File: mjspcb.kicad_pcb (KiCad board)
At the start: 2 copper layers, 97.2 x 55.9 mm, 77 parts, among them P10 Lipo, P2 serial breakout, P3 I2C breakout, P4 GPS, P5 piezo, P6 BPW34, P7 electrodes, P8 perfboard breakout, P9 reset, Q1 STU60N3LH5, Q2 STU60N3LH5, U1 ATMEGA328P, U2 RFM95W, U3 MCP1700-3302

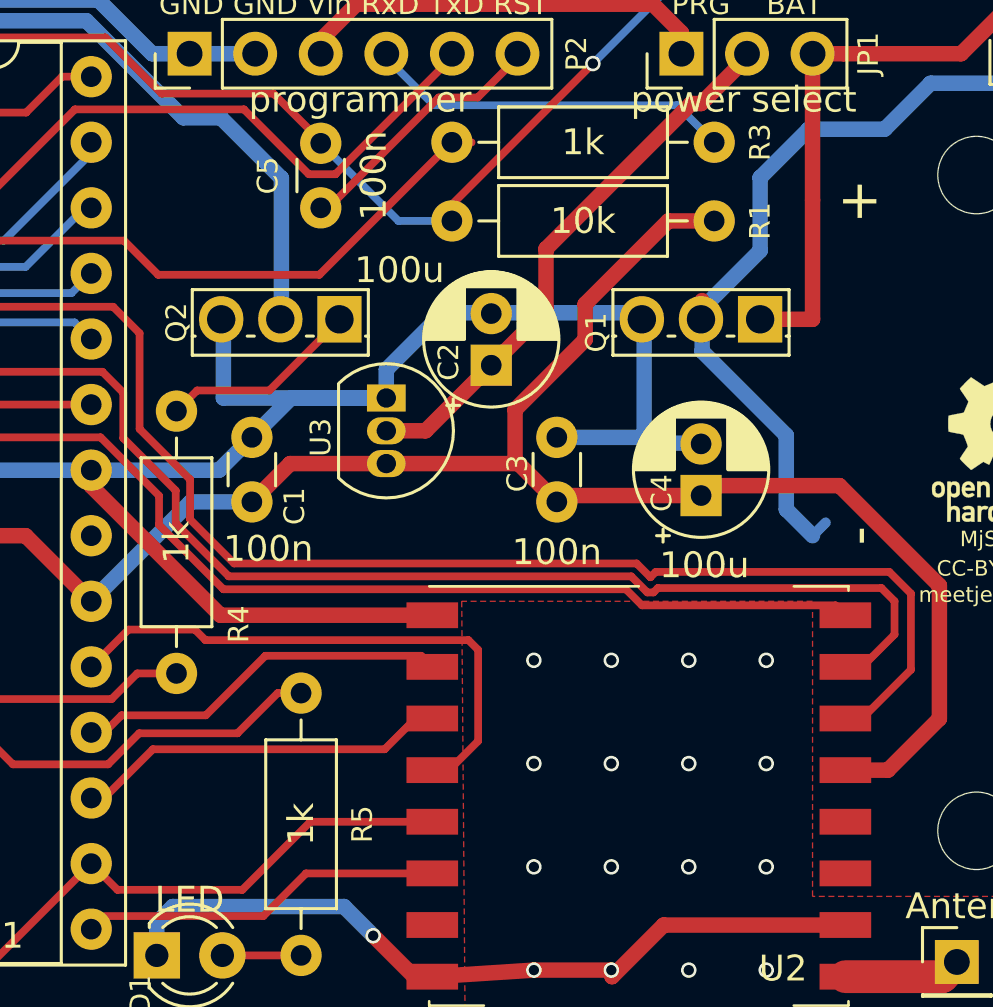
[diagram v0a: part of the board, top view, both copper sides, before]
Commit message: Re-add battery compartment
This was accidentally removed two commits ago.
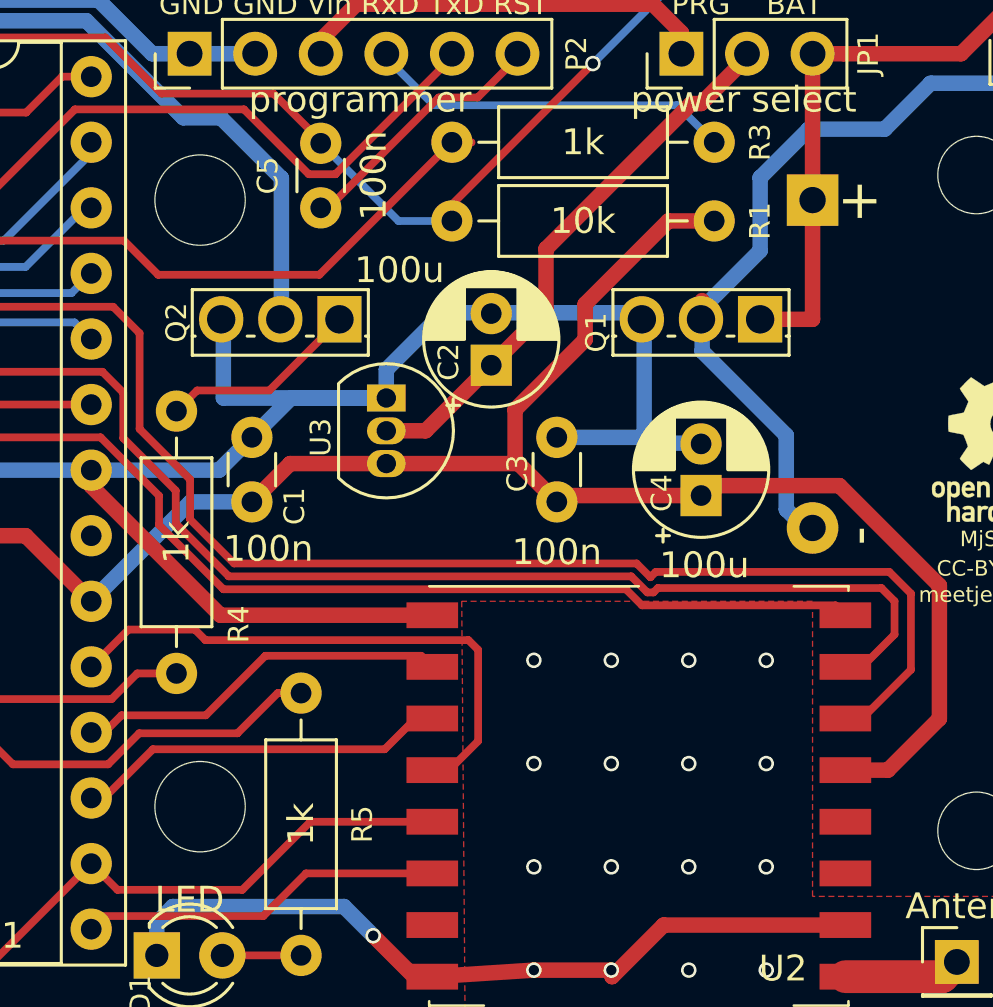
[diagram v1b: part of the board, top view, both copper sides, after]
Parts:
- added P1: Batteries, Battery:BatteryHolder_Keystone_2479_3xAAA, B.Cu at (209.6, 108.9)

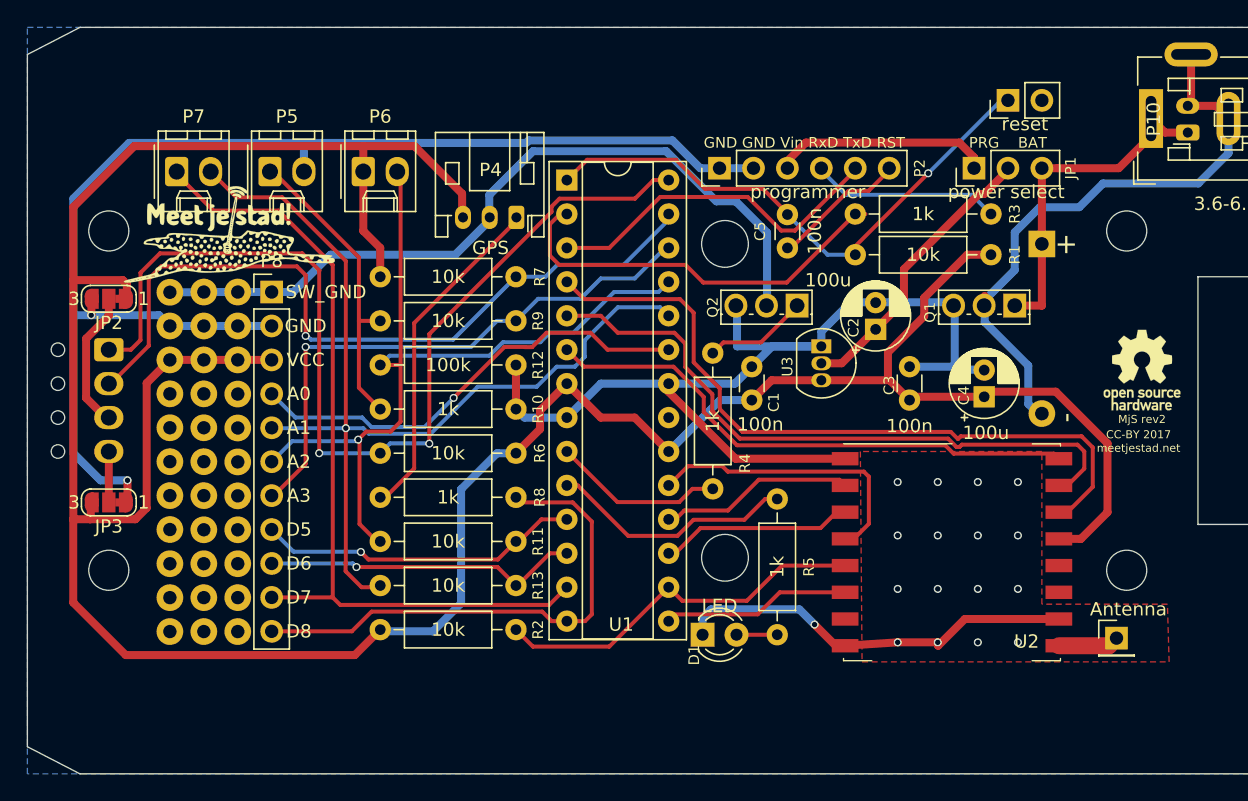
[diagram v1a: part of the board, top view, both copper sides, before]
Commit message: Add extra connectors to the board
This adds two connectors for dust sensors (SDS011 and HPMA115S0-XXX) and
two more generic grove connectors (digital and I²C). It also adds a long
pin header with assorted connections (I²C, SPI, various power) for use
with a piggy-back additional PCB which is expected to handle more
complex power needs.

For the grove connectors, some custom experimental footprints are added
that allow using the same footprint for both a 2.0mm grove connector and
a 2.54mm regular pin header.
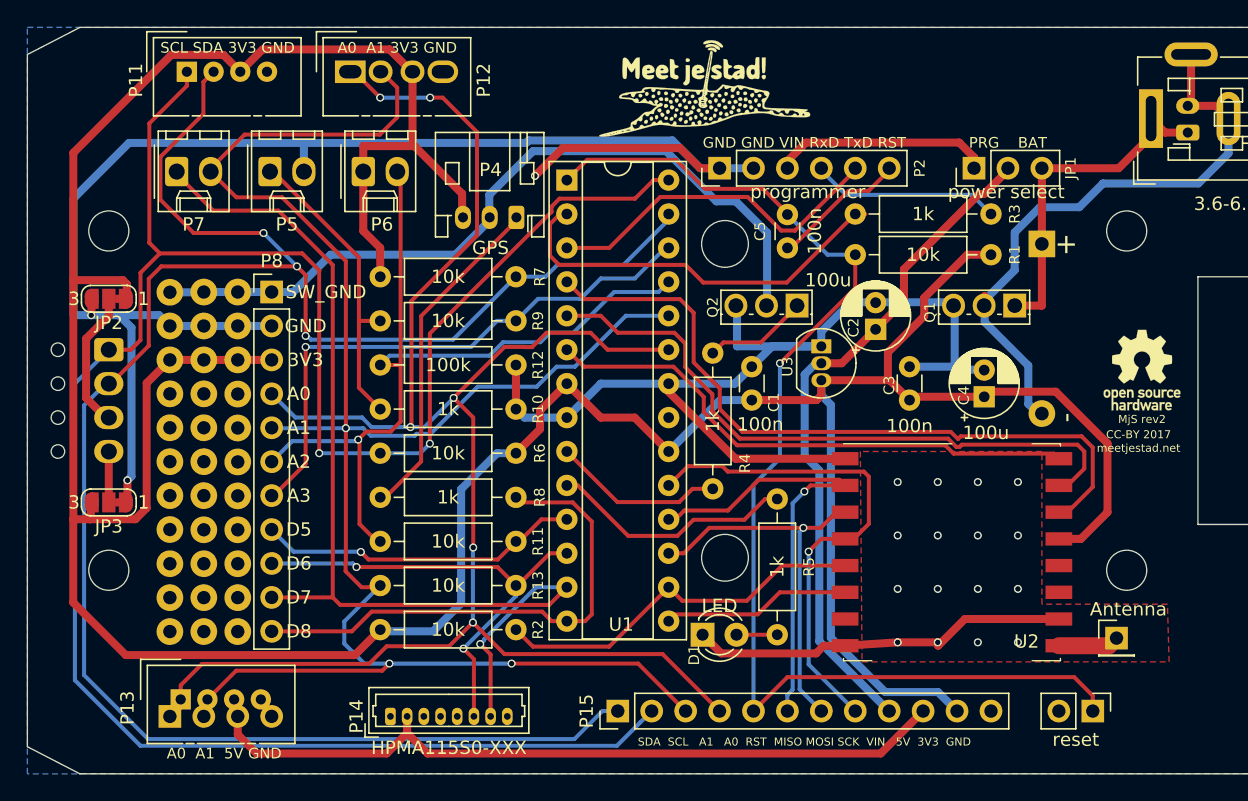
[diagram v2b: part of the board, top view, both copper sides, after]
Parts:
- added P11: grove i2c, Connector:NS-Tech_Grove_1x04_P2mm_Vertical, F.Cu at (145.5, 96.0)
- added P12: grove analog, meetjestad:NS-Tech_Grove_1x04_P2mm_P2.54mm_Vertical, F.Cu at (158.2, 96.0)
- added P13: grove analog, meetjestad:NS-Tech_Grove_1x04_P2mm_P2.54mm_Vertical_Alternative, F.Cu at (145.1, 143.0)
- added P14: HPMA115S0-XXX, Connector_Molex:Molex_PicoBlade_53047-0810_1x08_P1.25mm_Vertical, F.Cu at (160.8, 144.3)
- added P15: piggyback, Connector_PinHeader_2.54mm:PinHeader_1x12_P2.54mm_Vertical, F.Cu at (177.8, 143.9)
- moved P9 46.2 mm to (213.4, 143.9), turned to 270 degrees
- moved LOGO2 37.2 mm to (184.3, 97.3)
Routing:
- net A0: track 34.2 -> 134.9 mm, vias 1 -> 6
- net SDA: track 57.7 -> 146.8 mm, vias 1 -> 3
- net SCL: track 77.2 -> 164.4 mm
- net A1: track 74.0 -> 141.9 mm, vias 1 -> 3
- net 5V: track 0.00 -> 58.5 mm
- net RST: track 42.0 -> 91.2 mm
- net VCC: track 232.2 -> 280.6 mm
- net VIN: track 21.7 -> 51.2 mm
- net MISO: track 15.3 -> 35.5 mm, vias 0 -> 1
- net SCK: track 22.1 -> 38.6 mm, vias 0 -> 1
- net MOSI: track 14.5 -> 29.0 mm, vias 0 -> 1
- net D7: track 62.7 -> 76.7 mm, vias 0 -> 1
- net D6: track 23.8 -> 36.1 mm, vias 1 -> 2
- net GND: track 206.9 -> 218.0 mm
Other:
- board text added: "3V3"
- board text added: "A0 A1 3V3 GND"
- board text added: "A0 A1 5V GND"
- board text added: "GND GND VIN RxD TxD RST"
- board text added: "SCL SDA 3V3 GND"
- board text added: "SDA SCL A1 A0 RST MISO MOSI SCK VIN 5V 3V3 GND"
- board text removed: "GND GND Vin RxD TxD RST"
- board text removed: "VCC"

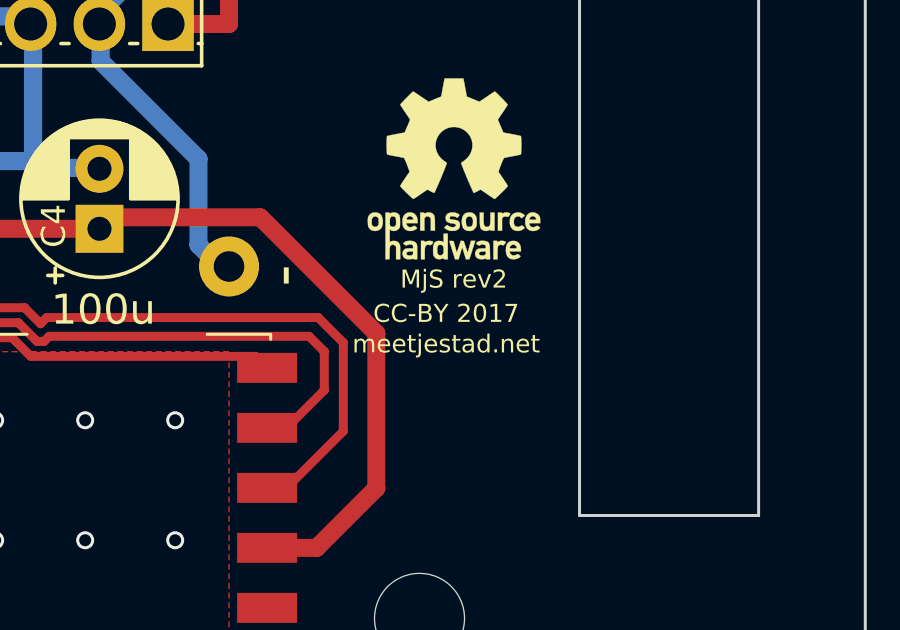
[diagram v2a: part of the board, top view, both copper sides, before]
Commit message: Merge text under OSHW logo in one element
Each of three lines were separate text objects, but you can also just
use newlines in a single text object.
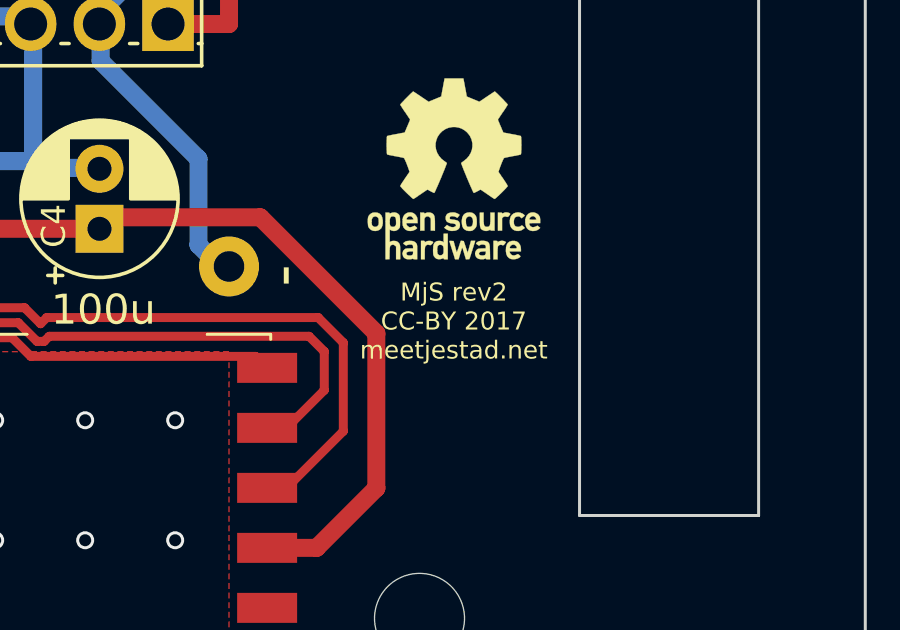
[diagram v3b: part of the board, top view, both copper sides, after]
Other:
- board text added: "MjS rev2 CC-BY 2017 meetjestad.net"
- board text removed: "CC-BY 2017"
- board text removed: "MjS rev2"
- board text removed: "meetjestad.net"
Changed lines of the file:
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@@
   (general
     (thickness 1.6)
-    (drawings 39)
+    (drawings 37)
     (tracks 677)
     (zones 0)
@@
     (effects (font (size 1 1) (thickness 0.25)))
   )
-  (gr_text "MjS rev2" (at 217.043 122.047) (layer F.SilkS)
-    (effects (font (size 0.6 0.6) (thickness 0.15)))
-  )
-  (gr_text meetjestad.net (at 216.789 124.206) (layer F.SilkS)
+  (gr_text "MjS rev2\nCC-BY 2017\nmeetjestad.net" (at 217.043 123.444) (layer F.SilkS)
     (effects (font (size 0.6 0.6) (thickness 0.15)))
   )
@@
     (effects (font (size 1.5 1.5) (thickness 0.3)) (justify mirror))
   )
-  (gr_text "CC-BY 2017" (at 216.789 123.19) (layer F.SilkS)
-    (effects (font (size 0.6 0.6) (thickness 0.15)))
-  )
   (gr_text D8 (at 153.924 137.922) (layer F.SilkS)

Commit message: Bump version and copyright year
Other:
- board text added: "MjS rev3 prototype1 CC-BY 2018 meetjestad.net"
- board text removed: "MjS rev2 CC-BY 2017 meetjestad.net"
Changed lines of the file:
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@@
     (effects (font (size 1 1) (thickness 0.25)))
   )
-  (gr_text "MjS rev2\nCC-BY 2017\nmeetjestad.net" (at 217.043 123.444) (layer F.SilkS)
+  (gr_text "MjS rev3\nprototype1\nCC-BY 2018\nmeetjestad.net" (at 217.043 124.206) (layer F.SilkS)
     (effects (font (size 0.6 0.6) (thickness 0.15)))
   )
